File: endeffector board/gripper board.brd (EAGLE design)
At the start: 63.5 x 63.2 mm, 40 parts, among them J1 APPPP45_PCB_HORIZ_RIGHT, J2 APPPP45_PCB_HORIZ_RIGHT, J3 APPPP45_PCB_HORIZ_RIGHT, J4 APPPP45_PCB_HORIZ_RIGHT, J5 APPPP45_PCB_HORIZ_RIGHT, Q1 MOSFET-NCHANNELFDD8780

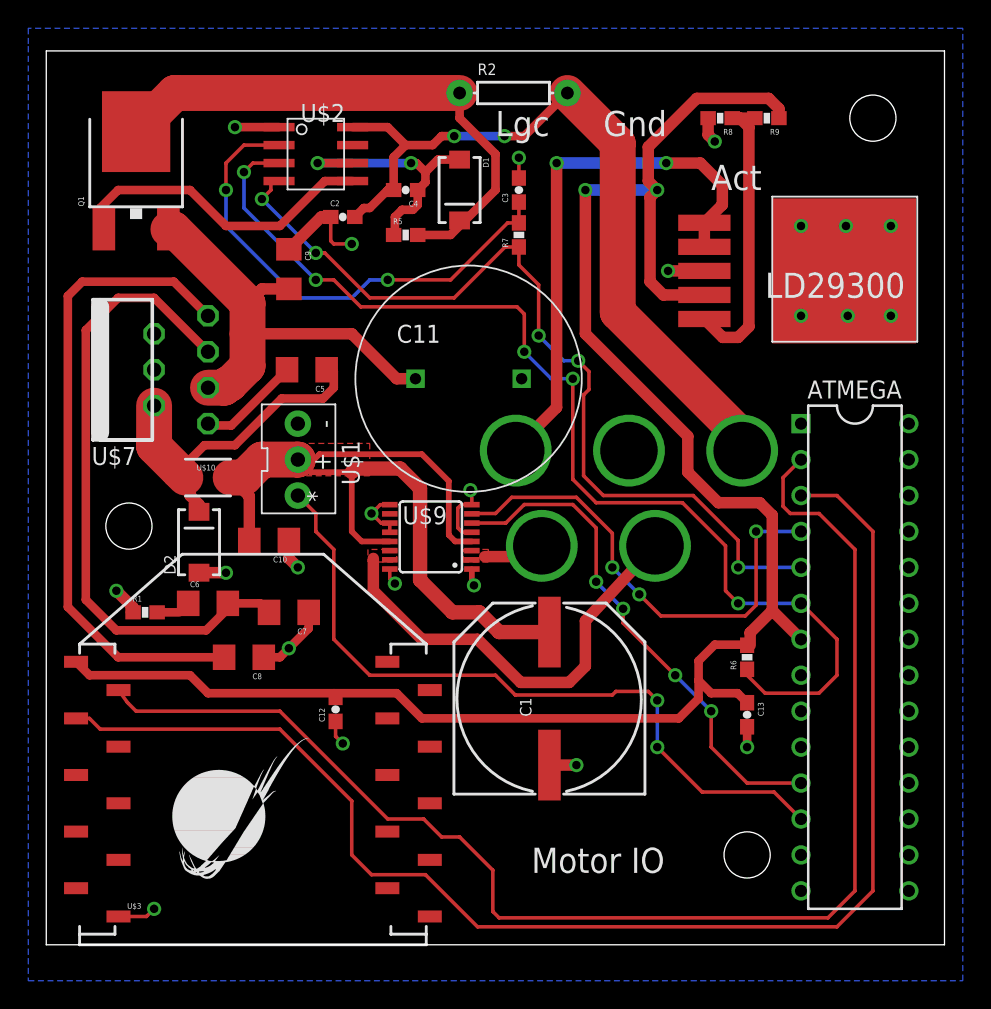
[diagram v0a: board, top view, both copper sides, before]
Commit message: end effector redesign
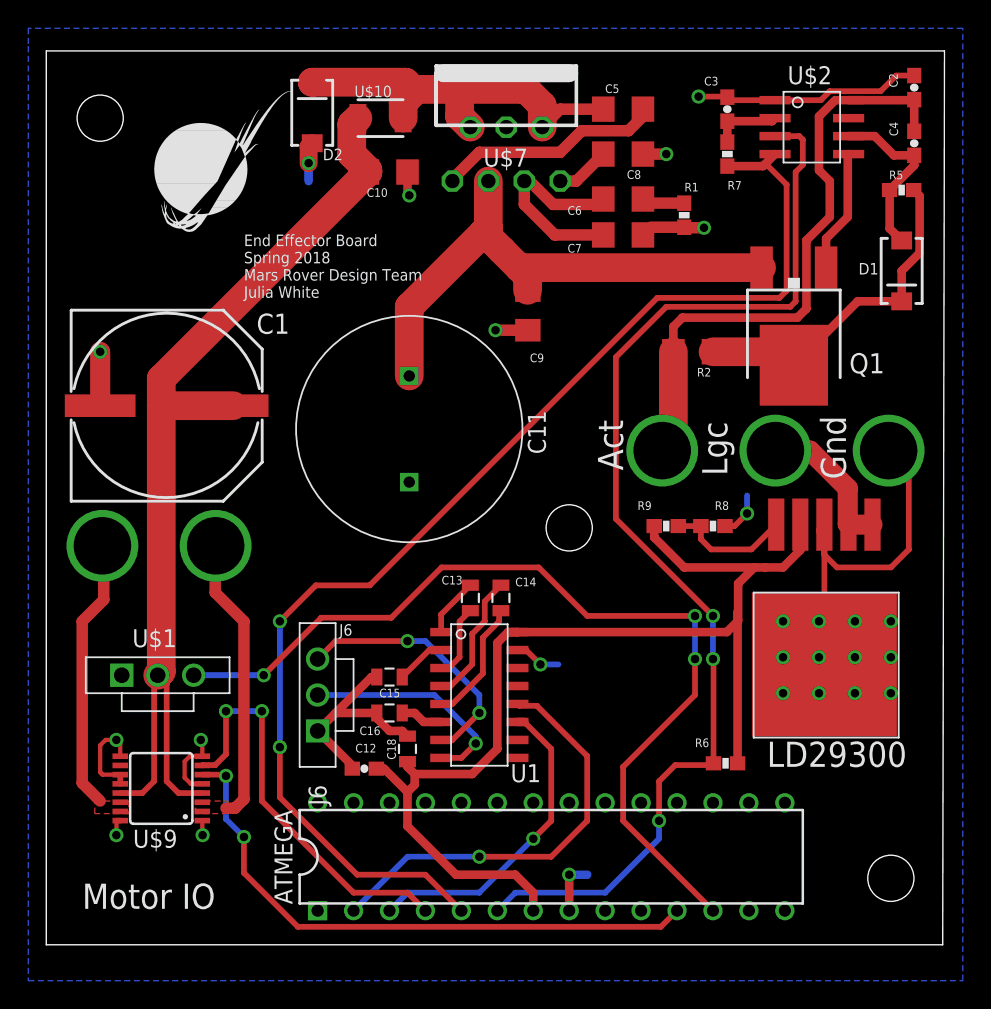
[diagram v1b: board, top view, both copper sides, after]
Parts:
- removed U$3: XBEE-1B3, SparkFun-RF:XBEE-SMD
- added C14, C15, C16, C18: .1uF, SparkFun-Capacitors:0805
- added J6: SL03, MRDT-Connectors:MOLEX-70543-0002
- added U1: MAX232D, MRDT-ICs:SOIC16
- C13: value 1uF -> .1uF; device SparkFun-Capacitors:0603-CAP -> SparkFun-Capacitors:0805
- R2: device SparkFun-Resistors:AXIAL-0.3 -> SparkFun-Resistors:1206
- U$1: value SERVO -> SERVOMOLEX_SL_VERT_TH; device MRDT-2015-General:SERVO_JACK -> MRDT-Connectors:MOLEX-70543-0002
- moved H3 59.3 mm to (59.7, 4.70)
- moved H2 54.6 mm to (3.81, 58.4), flipped to the bottom
- moved Q1 48.4 mm to (52.8, 42.5), turned to 180 degrees
- moved R1 47.3 mm to (45.1, 51.6), turned to 90 degrees
- moved J5 47.0 mm to (0.00, 0.00), flipped to the bottom
- moved LOGO1 45.7 mm to (7.62, 49.5)
- moved C8 44.5 mm to (40.8, 55.9)
- moved C2 41.4 mm to (61.3, 60.6), turned to 270 degrees
- moved C6 41.0 mm to (40.8, 52.7), turned to 180 degrees
- moved C4 36.1 mm to (61.3, 56.6), turned to 90 degrees
- moved C7 35.6 mm to (40.8, 50.2)
- moved R5 35.2 mm to (60.5, 53.3)
- moved U$2 35.1 mm to (54.1, 57.8)
- moved C1 34.1 mm to (8.51, 38.1), turned to 0 degrees
- moved D1 31.8 mm to (60.5, 47.6)
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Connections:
- removed net ATMEGA2XBEE: ATMEGA.3, U$3.3
- removed net XBEE2ATMEGA: ATMEGA.2, U$3.2
- new net ATMEGA2MAX: ATMEGA.3, U1.11
- new net MAX2ATMEGA: ATMEGA.2, U1.12
- new net N$13: C14.2, U1.5
- new net N$14: C14.1, U1.4
- new net N$15: C13.1, U1.1
- new net N$16: C15.1, U1.2
- new net N$17: C16.1, U1.6
- new net N$18: J6.3, U1.7
- new net N$19: J6.2, U1.8
- new net N$4: C13.2, U1.3
- net 5VIN: now also C18.1, U1.16; no longer C13.1, U$3.1
- net 5VMTR: now also U$1.2; no longer U$1.VCC
- net ACTPWR: now also R2.2; no longer R2.P$2
- net GND: now also C15.2, C16.2, C18.2, J6.1, U$1.1, U1.15; no longer C13.2, U$1.GND, U$3.10
- net N$9: now also R2.1; no longer R2.P$1
- net SERVOIN: now also U$1.3; no longer U$1.SIGNAL
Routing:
- net ATMEGA2XBEE: track 97.2 -> 0.00 mm
- net XBEE2ATMEGA: track 95.6 -> 0.00 mm
- net 5VIN: track 131.3 -> 81.4 mm, vias 2 -> 0
- net GND: track 57.4 -> 99.6 mm, vias 23 -> 14
- net N$8: track 45.8 -> 3.83 mm
- net N$10: track 45.3 -> 14.6 mm
- net N$1: track 35.2 -> 4.93 mm, vias 2 -> 0
- net MAX2ATMEGA: track 0.00 -> 30.2 mm, vias 0 -> 1
- net 12VLGC: track 38.8 -> 10.5 mm, vias 2 -> 0
- net MICROCNTRL: track 62.8 -> 90.2 mm, vias 5 -> 2
- net ATMEGA2MAX: track 0.00 -> 22.3 mm, vias 0 -> 1
- net N$18: track 0.00 -> 18.3 mm, vias 0 -> 2
- net MTR1_1: track 4.50 -> 20.3 mm
- net N$19: track 0.00 -> 15.8 mm, vias 0 -> 1
- net N$7: track 22.8 -> 8.68 mm
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- removed copper zone on layer 1, net 5VMTR
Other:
- outline, holes or cut-outs redrawn
- board text added: "End Effector Board Spring 2018 Mars Rover Design Team Julia White"
- board text added: "J6"

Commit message: Add files via upload
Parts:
- U$7: value SANC8050 -> SI-8050Y
- moved J3 16.0 mm to (63.5, 63.1)
- moved J1 15.9 mm to (47.6, 63.1)
- moved U$1 15.6 mm to (8.13, 34.7)
- moved C14 7.24 mm to (27.7, 18.8)
- moved C1 6.35 mm to (8.51, 44.5)
- moved U1 2.81 mm to (33.3, 18.5)
- moved R2 2.10 mm to (46.6, 43.8)
- moved Q1 2.10 mm to (53.7, 44.5)
- moved C11 2.07 mm to (24.1, 37.8)
- moved C13 1.83 mm to (31.5, 25.5), turned to 0 degrees
- moved LOGO1 1.80 mm to (6.35, 50.8)
- moved H2 1.27 mm to (3.81, 59.7)
- moved C6 1.17 mm to (41.5, 53.6)
- moved C7 1.17 mm to (41.5, 51.1)
- moved R1 1.17 mm to (45.8, 52.5)
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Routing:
- net 5VMTR: track 72.6 -> 91.8 mm
- net GND: track 99.6 -> 84.7 mm, vias 14 -> 25
- net ACTPWR: track 43.1 -> 52.3 mm
- net N$14: track 9.26 -> 3.10 mm
- net N$13: track 8.81 -> 2.89 mm
- net N$10: track 14.6 -> 18.4 mm
- net MICROCNTRL: track 90.2 -> 86.5 mm
- net N$18: track 18.3 -> 21.3 mm
- net N$19: track 15.8 -> 18.3 mm
- net N$17: track 3.01 -> 5.55 mm
- net N$16: track 3.54 -> 6.08 mm
- net N$9: track 24.8 -> 22.5 mm
- net N$7: track 8.68 -> 6.41 mm
- net N$15: track 4.17 -> 2.55 mm
- net ATMEGA2MAX: track 22.3 -> 23.7 mm
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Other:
- board size 63.5 x 63.2 mm -> 63.5 x 63.5 mm
- board text added: "End Effector Board Spring 2017 | Rev 1 Mars Rover Design Team Julia White"
- board text removed: "End Effector Board Spring 2018 Mars Rover Design Team Julia White"
